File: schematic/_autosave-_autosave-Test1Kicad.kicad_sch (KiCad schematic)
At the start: 28 parts, among them IC1 BMI055, U1 STM32F765IIKx, U2 NEO-M8N, U3 IST8310, U4 ICM-20602, U5 ICM-20689, U6 MS5611-01BA, U7 LT3080xDD, Y1 ABM2-8.000MHZ-D4Y-T

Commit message: Resistor change
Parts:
- added R1: 330k, symbol Device:R
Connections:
- net GND: now also R1.2
- net at U7.4 (SET): now also R1.1
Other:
- note added: "Voltage Regulator"
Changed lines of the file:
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@@
 	)
 	(rectangle
+		(start 248.92 200.66)
+		(end 293.37 233.68)
+		(stroke
+			(width 0)
+			(type default)
+		)
+		(fill
+			(type none)
+		)
+	)
+	(rectangle
 		(start 344.17 55.88)
 		(end 344.17 55.88)
@@
 		)
 	)
+	(text "Voltage Regulator"
+		(exclude_from_sim no)
+		(at 258.318 202.692 0)
+		(effects
+			(font
+				(size 1.27 1.27)
+			)
+		)
+	)
 	(text "Accel_Gyro_2"
 		(exclude_from_sim no)
@@
 	(wire
 		(pts
-			(xy 251.46 53.34) (xy 251.46 83.82)
+			(xy 359.41 189.23) (xy 367.03 189.23)
 		)
 		(stroke
@@
 	(wire
 		(pts
-			(xy 359.41 189.23) (xy 367.03 189.23)
+			(xy 346.71 152.4) (xy 349.25 152.4)
 		)
 		(stroke
@@
 	(wire
 		(pts
-			(xy 346.71 152.4) (xy 349.25 152.4)
+			(xy 384.81 200.66) (xy 384.81 203.2)
 		)
 		(stroke
@@
 	(wire
 		(pts
-			(xy 384.81 200.66) (xy 384.81 203.2)
+			(xy 261.62 217.17) (xy 261.62 219.71)
 		)
 		(stroke
@@
 	)
 	(symbol
+		(lib_id "Device:R")
+		(at 261.62 223.52 0)
+		(unit 1)
+		(exclude_from_sim no)
+		(in_bom yes)
+		(on_board yes)
+		(dnp no)
+		(fields_autoplaced yes)
+		(property "Reference" "R1"
+			(at 264.16 222.2499 0)
+			(effects
+				(font
+					(size 1.27 1.27)
+				)
+				(justify left)
+			)
+		)
+		(property "Value" "330k"
+			(at 264.16 224.7899 0)
+			(effects
+				(font
+					(size 1.27 1.27)
+				)
+				(justify left)
+			)
+		)
+		(property "Footprint" ""
+			(at 259.842 223.52 90)
+			(effects
+				(font
+					(size 1.27 1.27)
+				)
+				(hide yes)
+			)
+		)
+		(property "Datasheet" "~"
+			(at 261.62 223.52 0)
+			(effects
+				(font
+					(size 1.27 1.27)
+				)
+				(hide yes)
+			)
+		)
+		(property "Description" "Resistor"
+			(at 261.62 223.52 0)
+			(effects
+				(font
+					(size 1.27 1.27)
+				)
+				(hide yes)
+			)
+		)
+		(pin "2"
+		)
+		(pin "1"
+		)
+		(instances
+			(project ""
+				(path "/8ed38441-7d4e-4e89-870f-07e11c6dce38"
+					(reference "R1")
+					(unit 1)
+				)
+			)
+		)
+	)
+	(symbol
 		(lib_id "power:GND")
 		(at 308.61 130.81 0)
@@
 					(unit 1)
 				)
+			)
+		)
+	)
+	(symbol
+		(lib_id "power:GND")
+		(at 261.62 227.33 0)
+		(unit 1)
+		(exclude_from_sim no)
+		(in_bom yes)
+		(on_board yes)
+		(dnp no)
+		(fields_autoplaced yes)
+		(property "Reference" "#PWR016"
+			(at 261.62 233.68 0)
+			(effects
+				(font
+					(size 1.27 1.27)
+				)
+				(hide yes)
+			)
+		)
+		(property "Value" "GND"
+			(at 261.62 232.41 0)
+			(effects
+				(font
+					(size 1.27 1.27)
+				)
+			)
+		)
+		(property "Footprint" ""
+			(at 261.62 227.33 0)
+			(effects
+				(font
+					(size 1.27 1.27)
+				)
+				(hide yes)
+			)
+		)
+		(property "Datasheet" ""
+			(at 261.62 227.33 0)
+			(effects
+				(font
+					(size 1.27 1.27)
+				)
+				(hide yes)
+			)
+		)
+		(property "Description" "Power symbol creates a global label with name \"GND\" , ground"
+			(at 261.62 227.33 0)
+			(effects
+				(font
+					(size 1.27 1.27)
+				)
+				(hide yes)
+			)
+		)
+		(pin "1"
+		)
+		(instances
+			(project ""
+				(path "/8ed38441-7d4e-4e89-870f-07e11c6dce38"
+					(reference "#PWR016")
+					(unit 1)
+				)

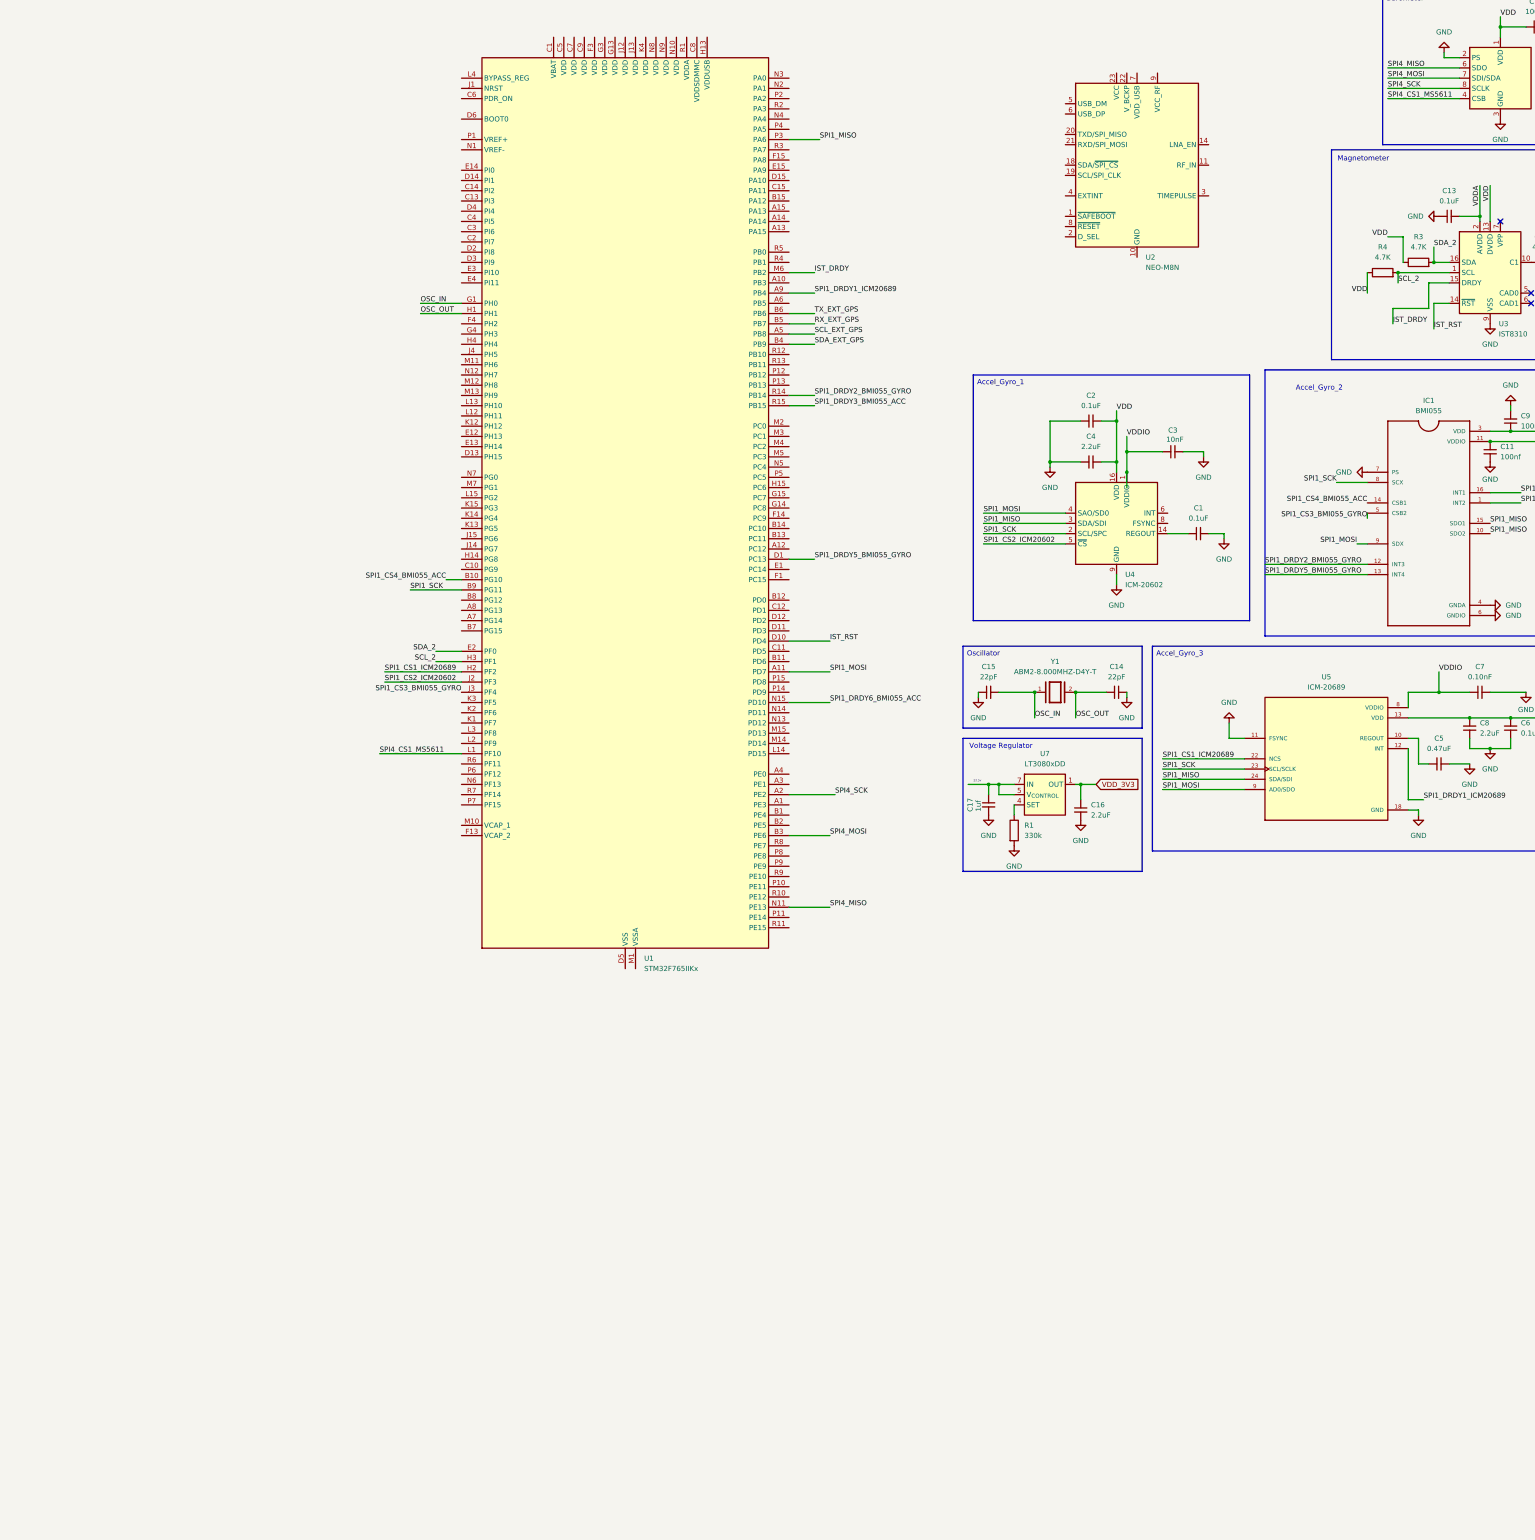
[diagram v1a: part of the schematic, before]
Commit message: Connectors
I added the Telemetry, Power, USB, and additional GPS connectors. I also added the I/O MCU for the connections to be linked to.
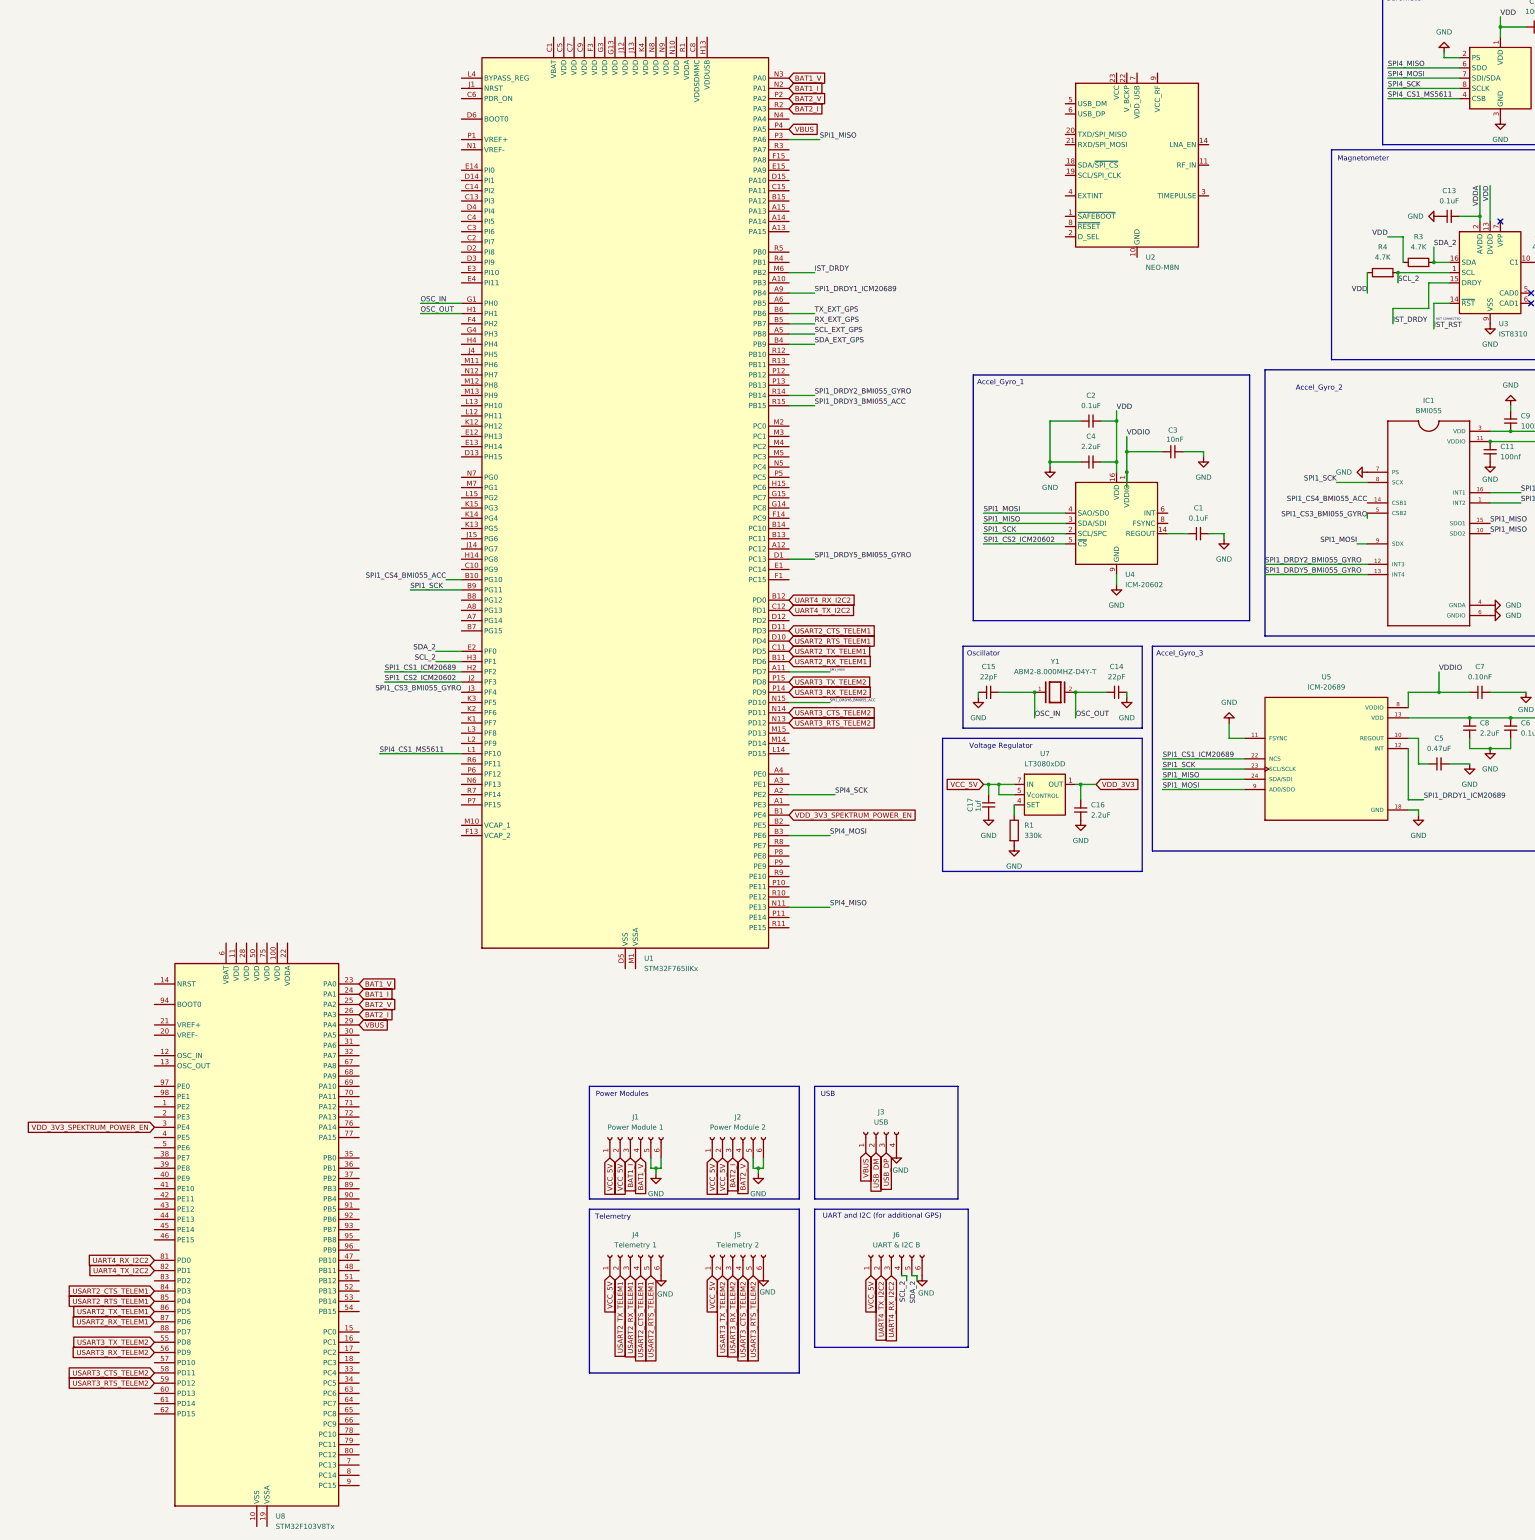
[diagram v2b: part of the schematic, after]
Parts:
- added J1: Power Module 1, Connector_JST:JST_GH_BM06B-GHS-TBT_1x06-1MP_P1.25mm_Vertical, symbol Connector:Conn_01x06_Socket
- added J2: Power Module 2, Connector_JST:JST_GH_BM06B-GHS-TBT_1x06-1MP_P1.25mm_Vertical, symbol Connector:Conn_01x06_Socket
- added J3: USB, Connector_JST:JST_GH_BM04B-GHS-TBT_1x04-1MP_P1.25mm_Vertical, symbol Connector:Conn_01x04_Socket
- added J4: Telemetry 1, Connector_JST:JST_GH_BM06B-GHS-TBT_1x06-1MP_P1.25mm_Vertical, symbol Connector:Conn_01x06_Socket
- added J5: Telemetry 2, Connector_JST:JST_GH_BM06B-GHS-TBT_1x06-1MP_P1.25mm_Vertical, symbol Connector:Conn_01x06_Socket
- added J6: UART & I2C B, Connector_JST:JST_GH_BM06B-GHS-TBT_1x06-1MP_P1.25mm_Vertical, symbol Connector:Conn_01x06_Socket
- added U8: STM32F103V8Tx, Package_QFP:LQFP-100_14x14mm_P0.5mm, symbol MCU_ST_STM32F1:STM32F103V8Tx
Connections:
- net GND: now also J1.5 (Pin_5), J1.6 (Pin_6), J2.5 (Pin_5), J2.6 (Pin_6), J3.4 (Pin_4), J4.6 (Pin_6), J5.6 (Pin_6), J6.6 (Pin_6)
- net IST_RST: no longer U1.D10 (PD4)
- net SCL_2: now also J6.4 (Pin_4)
- net SDA_2: now also J6.5 (Pin_5)
- net VDD_3V3_SPEKTRUM_POWER_EN: now reaches U1.B1 (PE4)
- net VDD_3V3_SPEKTRUM_POWER_EN: now also U8.3 (PE4)
- net USART2_RX_TELEM1: now reaches U1.B11 (PD6)
- net USART2_RX_TELEM1: now also J4.3 (Pin_3), U8.87 (PD6)
- net UART4_RX_I2C2: now reaches U1.B12 (PD0)
- net UART4_RX_I2C2: now also J6.3 (Pin_3), U8.81 (PD0)
- net USART2_TX_TELEM1: now reaches U1.C11 (PD5)
- net USART2_TX_TELEM1: now also J4.2 (Pin_2), U8.86 (PD5)
- net UART4_TX_I2C2: now reaches U1.C12 (PD1)
- net UART4_TX_I2C2: now also J6.2 (Pin_2), U8.82 (PD1)
- net USART2_CTS_TELEM1: now reaches U1.D11 (PD3)
- net USART2_CTS_TELEM1: now also J4.4 (Pin_4), U8.84 (PD3)
- net USART3_RTS_TELEM2: now reaches U1.N13 (PD12)
- net USART3_RTS_TELEM2: now also J5.5 (Pin_5), U8.59 (PD12)
- net USART3_CTS_TELEM2: now reaches U1.N14 (PD11)
- net USART3_CTS_TELEM2: now also J5.4 (Pin_4), U8.58 (PD11)
- net BAT1_I: now reaches U1.N2 (PA1)
- net BAT1_I: now also J1.3 (Pin_3), U8.24 (PA1)
- net BAT1_V: now reaches U1.N3 (PA0)
- net BAT1_V: now also J1.4 (Pin_4), U8.23 (PA0)
- net USART3_RX_TELEM2: now reaches U1.P14 (PD9)
- net USART3_RX_TELEM2: now also J5.3 (Pin_3), U8.56 (PD9)
- net USART3_TX_TELEM2: now reaches U1.P15 (PD8)
- net USART3_TX_TELEM2: now also J5.2 (Pin_2), U8.55 (PD8)
- net BAT2_V: now reaches U1.P2 (PA2)
- net BAT2_V: now also J2.4 (Pin_4), U8.25 (PA2)
- net VBUS: now reaches U1.P4 (PA5)
- net VBUS: now also J3.1 (Pin_1), U8.29 (PA4)
- net BAT2_I: now reaches U1.R2 (PA3)
- net BAT2_I: now also J2.3 (Pin_3), U8.26 (PA3)
- net VCC_5V: now reaches C17.1, U7.5 (V_{CONTROL}), U7.7 (IN), U7.8 (IN)
- net VCC_5V: now also J1.1 (Pin_1), J1.2 (Pin_2), J2.1 (Pin_1), J2.2 (Pin_2), J4.1 (Pin_1), J5.1 (Pin_1), J6.1 (Pin_1)
- new net: U8.10 (VSS), U8.27 (VSS), U8.49 (VSS), U8.74 (VSS), U8.99 (VSS)
- new net USART2_RTS_TELEM1: J4.5 (Pin_5), U1.D10 (PD4), U8.85 (PD4)
- new net USB_DM: J3.2 (Pin_2)
- new net USB_DP: J3.3 (Pin_3)
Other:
- note added: "NOT CONNECTED"
- note added: "Power Modules"
- note added: "Telemetry"
- note added: "UART and I2C (for additional GPS)"
- note added: "USB"
- note removed: "22.5v"

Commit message: CAN1,2 Transceiver and ports added
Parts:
- added J7: CAN 1, symbol Connector:Conn_01x04_Socket
- added J8: CAN 2, symbol Connector:Conn_01x04_Socket
- added U10, U9: TJA1051TK-3, Package_DFN_QFN:DFN-8-1EP_3x3mm_P0.65mm_EP1.55x2.4mm, symbol Interface_CAN_LIN:TJA1051TK-3
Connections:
- net GND: now also J7.4 (Pin_4), J8.4 (Pin_4), U10.2 (GND), U10.9 (GND), U9.2 (GND), U9.9 (GND)
- net VDD: now also U1.C5 (VDD)
- net VDDIO: now also U1.C7 (VDD), U10.5 (VIO), U9.5 (VIO)
- net CAN1_RX: now reaches U1.D3 (PI9)
- net CAN1_RX: now also U9.4 (RXD)
- net CAN1_TX: now reaches U1.E12 (PH13)
- net CAN1_TX: now also U9.1 (TXD)
- net CAN1_SILENT_S0: now reaches U1.F4 (PH2)
- net CAN1_SILENT_S0: now also U9.8 (S)
- net CAN2_RX/UART5_RX_ESC: now reaches U1.P12 (PB12)
- net CAN2_RX/UART5_RX_ESC: now also U10.4 (RXD)
- net CAN2_TX/UART5_TX_ESC: now reaches U1.P13 (PB13)
- net CAN2_TX/UART5_TX_ESC: now also U10.1 (TXD)
- new net: J8.2 (Pin_2), U10.7 (CANH)
- new net: J8.3 (Pin_3), U10.6 (CANL)
- new net: J7.2 (Pin_2), U9.7 (CANH)
- new net: J7.3 (Pin_3), U9.6 (CANL)
- new net CAN2_SILENT_S1: U10.8 (S)
